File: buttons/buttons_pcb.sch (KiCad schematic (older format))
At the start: 1 part, among them J1 Conn_01x02

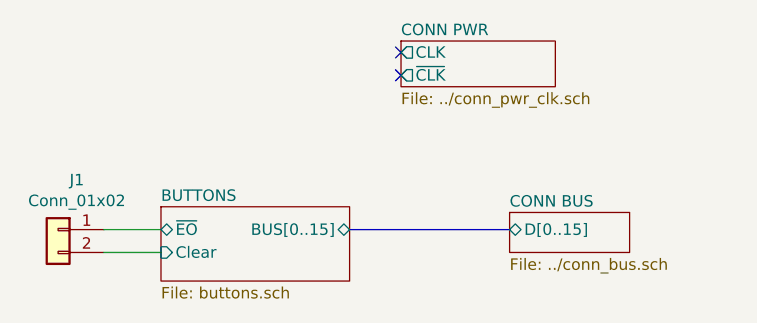
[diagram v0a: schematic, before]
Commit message: add bit operations
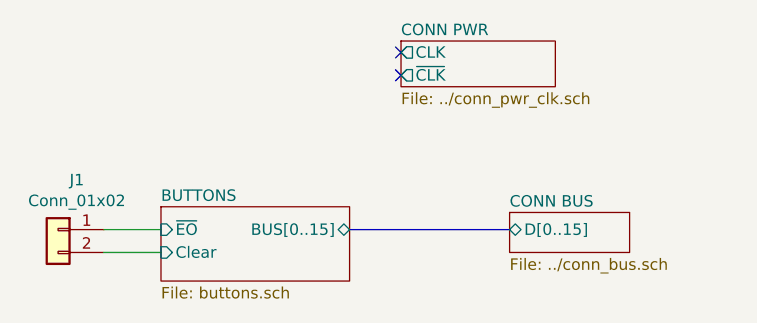
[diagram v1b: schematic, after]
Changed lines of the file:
@@
 EESchema Schematic File Version 4
+LIBS:buttons_pcb-cache
 EELAYER 30 0
 EELAYER END
@@
 F1 "buttons.sch" 50
 F2 "Clear" I L 4775 2675 50
-F3 "~EO~" B L 4775 2575 50
+F3 "~EO~" I L 4775 2575 50
 F4 "BUS[0..15]" B R 5600 2575 50
 $EndSheet
